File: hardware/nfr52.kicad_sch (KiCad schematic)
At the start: 46 parts, among them J1 USB_C_Receptacle_USB2.0_14P, J10 U.FL, J2 Conn_01x10, J3 Conn_01x10, J4 Conn_01x03, U3 nRF52820-QDxx, U4 TPS63900, Y2 32MHz

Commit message: Stash
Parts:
- added JP4: SolderJumper_2_Open, PCM_ckl-misc:SolderJumper-2_Open_Pad_Small, symbol Jumper:SolderJumper_2_Open
- added SW3: SW_Push, nrf54:SW_Push_SPST_TSA016, symbol Switch:SW_Push
- C14, C15: LCSC Part # (none) -> C106199
- C22, C23, C41: LCSC Part # (none) -> C380302
- C24, C40: LCSC Part # (none) -> C519560
- C25, C26, C37: LCSC Part # (none) -> C60474
- C27, C28: LCSC Part # (none) -> C7432767
- C35: LCSC Part # (none) -> C85893
- C36: LCSC Part # (none) -> C22374839
- C38: LCSC Part # (none) -> C541383
- C39: LCSC Part # (none) -> C272875
- H1, JP2, JP3: now not fitted
- J1: footprint Connector_USB:USB_C_Receptacle_HRO_TYPE-C-31-M-12 -> PCM_ckl-connector:USB_C_Receptacle_HRO_TYPE-C-31-M-12; LCSC Part # C393939 -> C2681555
- J10: LCSC Part # (none) -> C88374
- J2, J3: footprint Connector_PinHeader_2.54mm:PinHeader_1x10_P2.54mm_Vertical -> nrf54:Castellated_1x10_P2.54mm_Vertical; now not fitted; now left out of the parts list
- J4, TP1, TP10, TP2, TP3, TP4: now not fitted; now left out of the parts list
- L10: LCSC Part # C22471111 -> C5832372
- L6: LCSC Part # (none) -> C281107
- L7: LCSC Part # (none) -> C86059
- L8: LCSC Part # (none) -> C86126
- L9: LCSC Part # (none) -> C98041
- R10: LCSC Part # (none) -> C49010116
- R11: LCSC Part # (none) -> C2906900
- R12, R13: LCSC Part # (none) -> C852856
- R3, R4, R5, R6, R7: LCSC Part # (none) -> C2906931
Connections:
- net GND: now also SW3.2
- net P0.06: now also SW3.1
- net SEL: now also JP4.1 (A)
- net VBUS: now also JP4.2 (B)

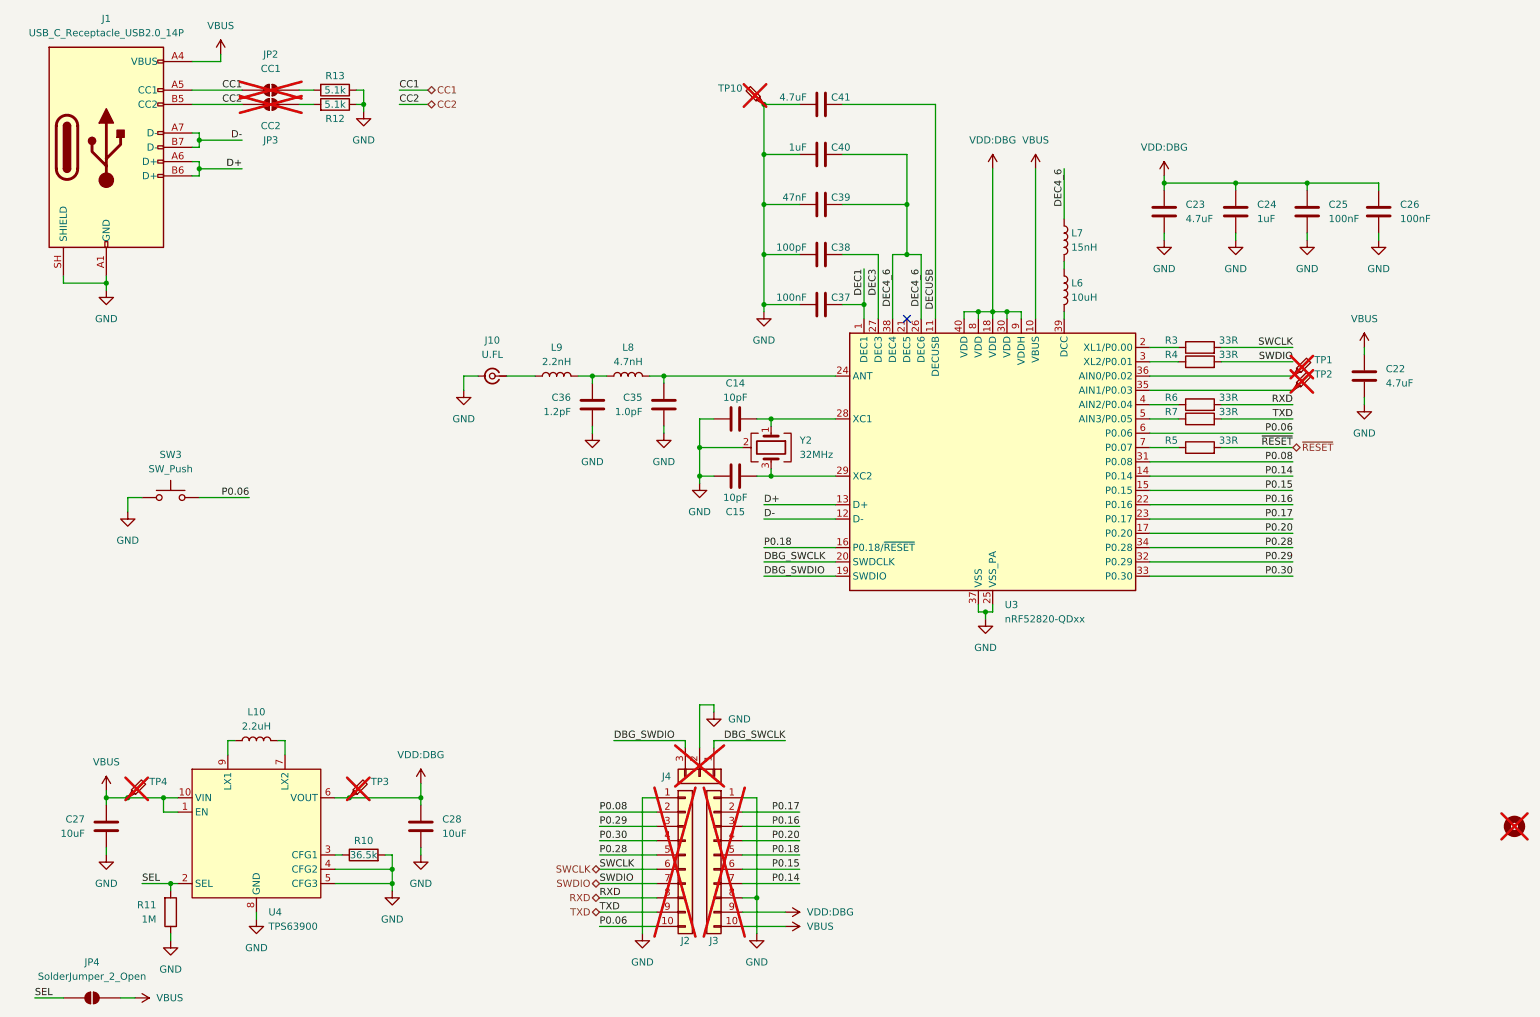
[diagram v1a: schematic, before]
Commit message: Add schematic
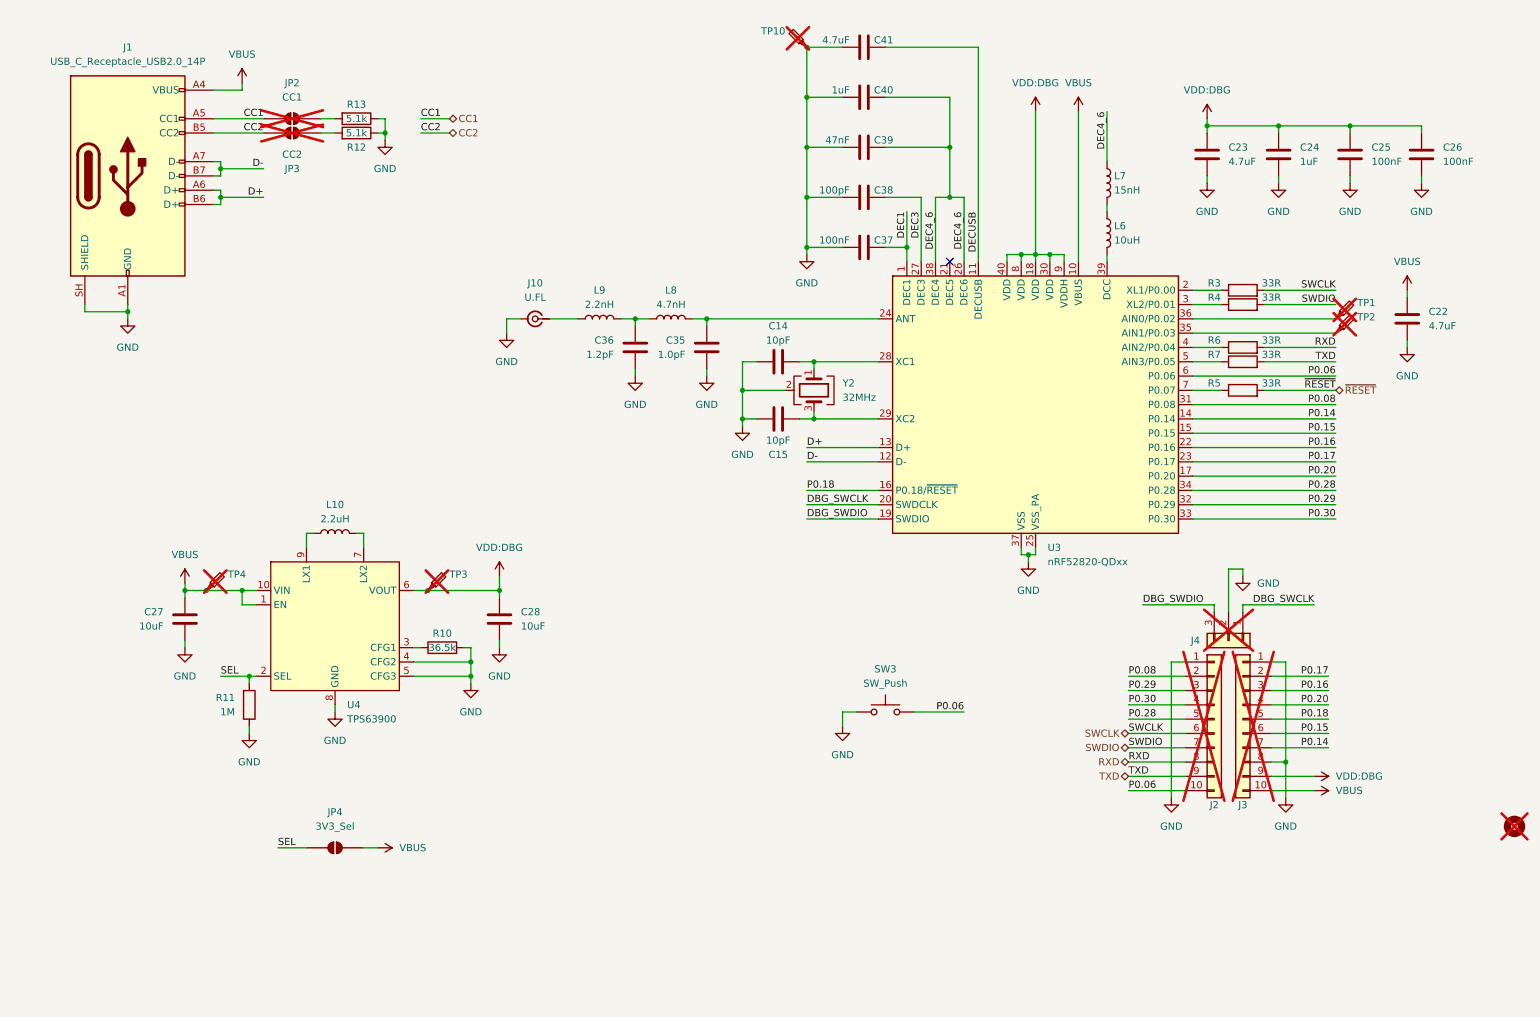
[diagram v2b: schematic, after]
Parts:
- JP4: value SolderJumper_2_Open -> 3V3_Sel
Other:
- title: (none) -> nRF54L15 Discovery
- moved on the sheet: C14, C15, C22, C23, C24, C25, C26, C27, C28, C35, C36, C37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
